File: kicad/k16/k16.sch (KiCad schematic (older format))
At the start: 327 parts, among them J1 PCIEPWR, J3 PINHD-1X4, J5 PINHD-1X4, Q1 NDS351AN, U1 AVALON, U10 AVALON, U11 AVALON, U12 AVALON, U13 AVALON, U14 AVALON, U15 AVALON, U16 AVALON, U17 PIC16LF1459, U18 IR3895, U19 IR3895, U2 AVALON, U20 MCP16321, U21 NL27WZ14, U22 AP7217D / RT9166A, U23 AP7172D / RT9166A, U24 74AUP1G02, U3 AVALON, U4 AVALON, U5 AVALON, U6 AVALON, U7 AVALON, U8 AVALON, U9 AVALON, X1 ASMDB

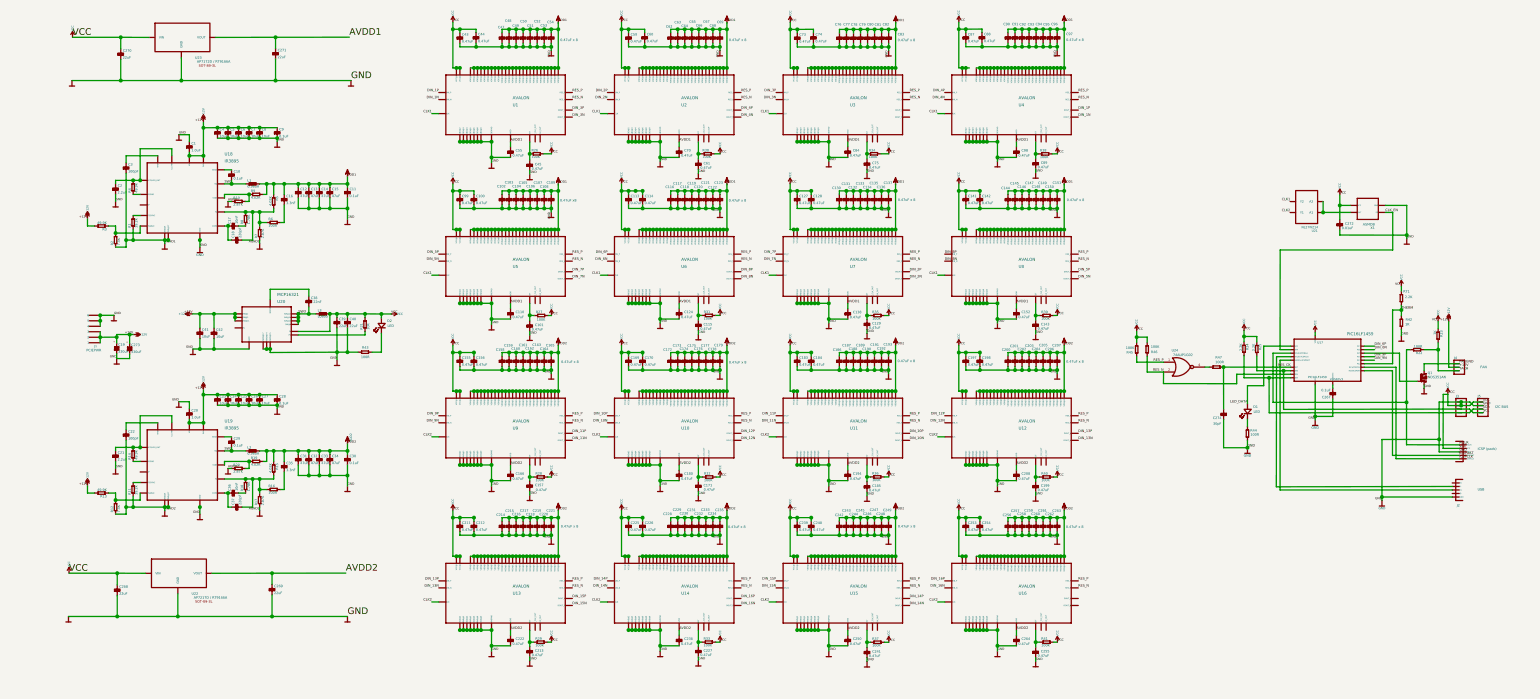
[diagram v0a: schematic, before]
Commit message: update K16 brd for PIC VCC fix, 0.2.1
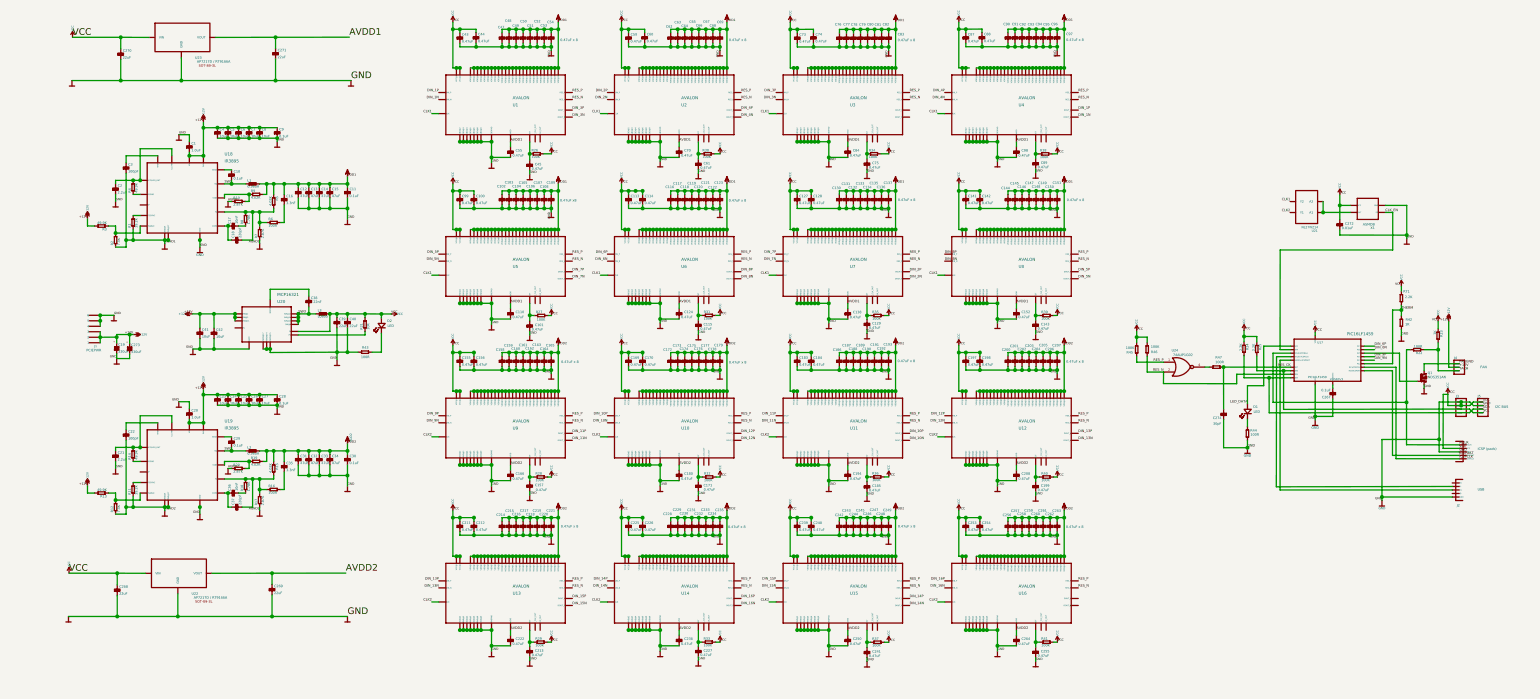
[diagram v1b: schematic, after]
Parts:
- U23: value AP7172D / RT9166A -> AP7217D / RT9166A
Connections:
- net VCC: now also U17.1 (VDD)
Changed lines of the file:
@@
-EESchema Schematic File Version 2  date Thu 30 May 2013 09:22:30 AM ICT
+EESchema Schematic File Version 2  date Fri 21 Jun 2013 07:32:08 AM ICT
 LIBS:k16
 LIBS:power
@@
 encoding utf-8
 Sheet 1 1
-Title "asic-v1.sch"
-Date "30 may 2013"
+Title "Klondike 16 ASIC Miner"
+Date "21 jun 2013"
 Rev ""
 Comp ""
@@
 L VDD1 #VDD061
 U 1 1 517F6E0B
-P 6647 2641
-F 0 "#VDD061" V 6615 2610 22  0001 L BNN
-F 1 "VDD1" H 6647 2641 60  0001 C CNN
-F 2 "" H 6647 2641 60  0001 C CNN
-F 3 "" H 6647 2641 60  0001 C CNN
-	1    6647 2641
+P 6647 2631
+F 0 "#VDD061" V 6615 2600 22  0001 L BNN
+F 1 "VDD1" H 6647 2631 60  0001 C CNN
+F 2 "" H 6647 2631 60  0001 C CNN
+F 3 "" H 6647 2631 60  0001 C CNN
+	1    6647 2631
 	1    0    0    -1
 $EndComp
@@
 L VDD1 #VDD062
 U 1 1 517F6E07
-P 6647 4113
-F 0 "#VDD062" V 6615 4082 22  0001 L BNN
-F 1 "VDD1" H 6647 4113 60  0001 C CNN
-F 2 "" H 6647 4113 60  0001 C CNN
-F 3 "" H 6647 4113 60  0001 C CNN
-	1    6647 4113
+P 6647 4103
+F 0 "#VDD062" V 6615 4072 22  0001 L BNN
+F 1 "VDD1" H 6647 4103 60  0001 C CNN
+F 2 "" H 6647 4103 60  0001 C CNN
+F 3 "" H 6647 4103 60  0001 C CNN
+	1    6647 4103
 	1    0    0    -1
 $EndComp
@@
 L VDD1 #VDD063
 U 1 1 517F6E06
-P 8183 4113
-F 0 "#VDD063" V 8151 4082 22  0001 L BNN
-F 1 "VDD1" H 8183 4113 60  0001 C CNN
-F 2 "" H 8183 4113 60  0001 C CNN
-F 3 "" H 8183 4113 60  0001 C CNN
-	1    8183 4113
+P 8183 4103
+F 0 "#VDD063" V 8151 4072 22  0001 L BNN
+F 1 "VDD1" H 8183 4103 60  0001 C CNN
+F 2 "" H 8183 4103 60  0001 C CNN
+F 3 "" H 8183 4103 60  0001 C CNN
+	1    8183 4103
 	1    0    0    -1
 $EndComp
@@
 L VDD1 #VDD064
 U 1 1 517F6DF8
-P 9719 4113
-F 0 "#VDD064" V 9687 4082 22  0001 L BNN
-F 1 "VDD1" H 9719 4113 60  0001 C CNN
-F 2 "" H 9719 4113 60  0001 C CNN
-F 3 "" H 9719 4113 60  0001 C CNN
-	1    9719 4113
+P 9719 4103
+F 0 "#VDD064" V 9687 4072 22  0001 L BNN
+F 1 "VDD1" H 9719 4103 60  0001 C CNN
+F 2 "" H 9719 4103 60  0001 C CNN
+F 3 "" H 9719 4103 60  0001 C CNN
+	1    9719 4103
 	1    0    0    -1
 $EndComp
@@
 L VDD1 #VDD065
 U 1 1 517F6E04
-P 11255 4113
-F 0 "#VDD065" V 11223 4082 22  0001 L BNN
-F 1 "VDD1" H 11255 4113 60  0001 C CNN
-F 2 "" H 11255 4113 60  0001 C CNN
-F 3 "" H 11255 4113 60  0001 C CNN
-	1    11255 4113
+P 11255 4103
+F 0 "#VDD065" V 11223 4072 22  0001 L BNN
+F 1 "VDD1" H 11255 4103 60  0001 C CNN
+F 2 "" H 11255 4103 60  0001 C CNN
+F 3 "" H 11255 4103 60  0001 C CNN
+	1    11255 4103
 	1    0    0    -1
 $EndComp
@@
 L VDD1 #VDD0104
 U 1 1 518D82F1
-P 8183 2641
-F 0 "#VDD0104" V 8151 2610 22  0001 L BNN
-F 1 "VDD1" H 8183 2641 60  0001 C CNN
-F 2 "" H 8183 2641 60  0001 C CNN
-F 3 "" H 8183 2641 60  0001 C CNN
-	1    8183 2641
+P 8183 2631
+F 0 "#VDD0104" V 8151 2600 22  0001 L BNN
+F 1 "VDD1" H 8183 2631 60  0001 C CNN
+F 2 "" H 8183 2631 60  0001 C CNN
+F 3 "" H 8183 2631 60  0001 C CNN
+	1    8183 2631
 	1    0    0    -1
 $EndComp
@@
 L VDD1 #VDD0107
 U 1 1 518D8547
-P 9720 2642
-F 0 "#VDD0107" V 9688 2611 22  0001 L BNN
-F 1 "VDD1" H 9720 2642 60  0001 C CNN
-F 2 "" H 9720 2642 60  0001 C CNN
-F 3 "" H 9720 2642 60  0001 C CNN
-	1    9720 2642
+P 9720 2632
+F 0 "#VDD0107" V 9688 2601 22  0001 L BNN
+F 1 "VDD1" H 9720 2632 60  0001 C CNN
+F 2 "" H 9720 2632 60  0001 C CNN
+F 3 "" H 9720 2632 60  0001 C CNN
+	1    9720 2632
 	1    0    0    -1
 $EndComp
@@
 L VDD1 #VDD0110
 U 1 1 518D879D
-P 11255 2640
-F 0 "#VDD0110" V 11223 2609 22  0001 L BNN
-F 1 "VDD1" H 11255 2640 60  0001 C CNN
-F 2 "" H 11255 2640 60  0001 C CNN
-F 3 "" H 11255 2640 60  0001 C CNN
-	1    11255 2640
+P 11255 2630
+F 0 "#VDD0110" V 11223 2599 22  0001 L BNN
+F 1 "VDD1" H 11255 2630 60  0001 C CNN
+F 2 "" H 11255 2630 60  0001 C CNN
+F 3 "" H 11255 2630 60  0001 C CNN
+	1    11255 2630
 	1    0    0    -1
 $EndComp
@@
 P 3224 2819
 F 0 "U23" H 3369 2634 22  0000 C CNN
-F 1 "AP7172D / RT9166A" H 3508 2599 22  0000 C CNN
+F 1 "AP7217D / RT9166A" H 3508 2599 22  0000 C CNN
 F 2 "~" H 3224 2819 60  0000 C CNN
 F 3 "~" H 3224 2819 60  0000 C CNN
@@
 	15068 6140 14981 6140
 Wire Wire Line
-	14950 6172 14981 6140
+	14981 6140 14950 6172
 Wire Wire Line
 	15068 6172 14983 6173
 Wire Wire Line
-	14950 6140 14983 6173
+	14983 6173 14950 6140
 Wire Wire Line
-	14670 6140 14870 6140
+	14950 6140 14870 6140
 Wire Wire Line
-	14870 6140 14950 6140
+	14870 6140 14670 6140
 Wire Wire Line
-	14749 6172 14870 6172
+	14950 6172 14870 6172
 Wire Wire Line
-	14870 6172 14950 6172
+	14870 6172 14749 6172
 Connection ~ 14870 6140
 Connection ~ 14870 6172
@@
 	9720 2746 9720 2682
 Wire Wire Line
-	9720 2746 9719 3097
+	9719 3097 9720 2746
 Wire Wire Line
 	9208 2778 9208 2746
@@
 	12535 5822 12578 5822
 Connection ~ 12706 5822
+Text Label 13541 5503 0    22   ~ 0
+VCC
 $EndSCHEMATC

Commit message: update resistors, parts list, v0.2.2
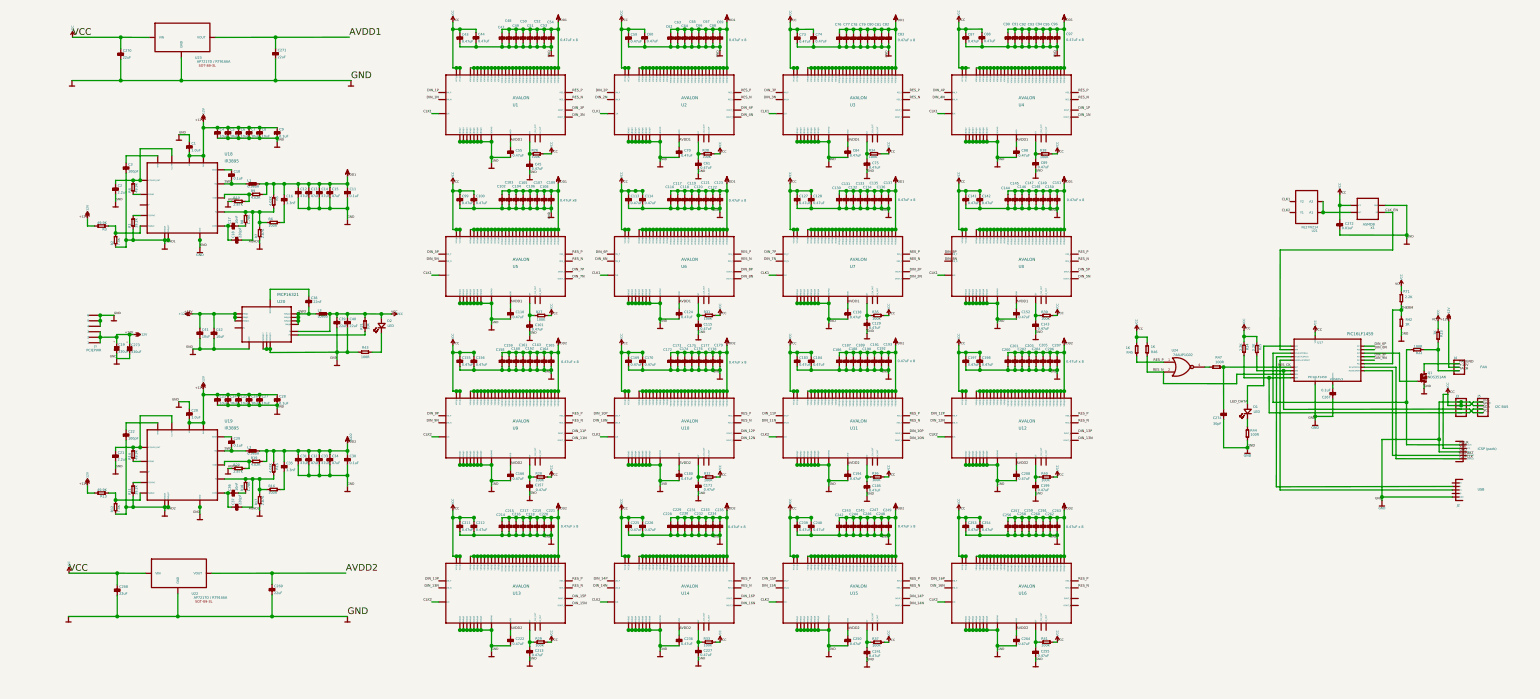
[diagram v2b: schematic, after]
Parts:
- R45, R46: value 100K -> 1K

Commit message: beta final 0.3.0 release
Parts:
- removed U24: 74AUP1G02, ~, symbol 74AUP1G02
- added C275: 0.01uF, symbol C-EU
- added C276: 0.1uF, symbol C-EU
- added D3: SL02, ~, symbol DIODE
- added L10, L11, L12, L13, L14, L15, L16, L17, L18, L19, L4, L5, L6, L7, L8, L9: FB, symbol R-EU
- added L20, L22: 120R @ 100 MHz, symbol R-EU
- added L21: 120R / 100 MHz, symbol R-EU
- added L23: 220R / 100 MHz, symbol R-EU
- added R48: 1K, symbol R-EU
- added unit 1 of U21
- added U24: 74AUP2G02, ~, symbol 74AUP2G02
- added U25: NL27WZ14, symbol NL27WZ14
- C109: value 0.47uF x8 -> 0.47uF
- C123, C137, C151, C165, C179, C193, C207, C221, C235, C249, C263, C54, C69, C83, C97: value 0.47uF x 8 -> 0.47uF
- U21: symbol NL27W -> NL27WZ14
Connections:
- net +12V: now also D3.2 (K)
- net AVDD1: now also L10.1, L11.1, L4.1, L5.1, L6.1, L7.1, L8.1, L9.1; no longer C110.1, C124.1, C138.1, C152.1, C55.1, C70.1, C84.1, C98.1, U1.P$42 (AVDD), U2.P$42 (AVDD), U3.P$42 (AVDD), U4.P$42 (AVDD), U5.P$42 (AVDD), U6.P$42 (AVDD), U7.P$42 (AVDD), U8.P$42 (AVDD)
- net AVDD2: now also L12.1, L13.1, L14.1, L15.1, L16.1, L17.1, L18.1, L19.1; no longer C166.1, C180.1, C194.1, C208.1, C222.1, C236.1, C250.1, C264.1, U10.P$42 (AVDD), U11.P$42 (AVDD), U12.P$42 (AVDD), U13.P$42 (AVDD), U14.P$42 (AVDD), U15.P$42 (AVDD), U16.P$42 (AVDD), U9.P$42 (AVDD)
- net CLK2: now also U21.6; no longer U21.6 (Y1)
- net FANGND: now also D3.1 (A)
- net GND: now also C275.2, C276.1, L22.1, L23.1, R48.2, U21.2 (GND), U24.4 (GND), U24.4 (GND), U25.2 (GND), U25.2 (GND); no longer J2.5 (GND), J2.S1 (GND), J2.S2 (GND), J2.S3 (GND), J2.S4 (GND)
- net RES_CK: now also U25.4; no longer C274.2, R47.2
- net RES_N: now also U24.2 (B), U25.1; no longer U17.12 (RB5)
- net RES_P: now also U24.1 (A)
- net VCC: now also C275.1, C276.2, U21.5 (VCC), U24.8 (VCC), U24.8 (VCC), U25.5 (VCC), U25.5 (VCC)
- net at U21.3, X1.3 (OUT): now also U21.1; no longer U21.1 (A1)
- net at U17.18 (RA1/D-/ICSPCLK): now also L20.1; no longer J2.2 (D-)
- net at U17.19 (RA0/D+/ICSPDAT): now also L21.1; no longer J2.3 (D+)
- net at Q1.3 (G), U17.5 (RC5): now also R48.1
- net at R47.1: now also C274.2, U24.5 (A)
- new net: C222.1, L16.2, U13.P$42 (AVDD)
- new net: C208.1, L15.2, U12.P$42 (AVDD)
- new net: C194.1, L14.2, U11.P$42 (AVDD)
- new net: C180.1, L13.2, U10.P$42 (AVDD)
- new net: C166.1, L12.2, U9.P$42 (AVDD)
- new net: C152.1, L11.2, U8.P$42 (AVDD)
- new net: C138.1, L10.2, U7.P$42 (AVDD)
- new net: C124.1, L9.2, U6.P$42 (AVDD)
- new net: C110.1, L8.2, U5.P$42 (AVDD)
- new net: C98.1, L7.2, U4.P$42 (AVDD)
- new net: C84.1, L6.2, U3.P$42 (AVDD)
- new net: C70.1, L5.2, U2.P$42 (AVDD)
- new net: C55.1, L4.2, U1.P$42 (AVDD)
- new net: C236.1, L17.2, U14.P$42 (AVDD)
- new net: C264.1, L19.2, U16.P$42 (AVDD)
- new net: C250.1, L18.2, U15.P$42 (AVDD)
- new net: J2.5 (GND), J2.S1 (GND), J2.S2 (GND), J2.S3 (GND), J2.S4 (GND), L22.2, L23.2
- new net: U24.3 (Y), U25.3
- new net D+: J2.3 (D+), L21.2
- new net D-: J2.2 (D-), L20.2
- new net RES_DI: U17.12 (RB5), U25.6
- new net RES_PN: R47.2, U24.6 (B), U24.7 (Y)
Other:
- moved on the sheet: C1, C10, C100, C101, C102, C103, C104, C105, C106, C107, C108, C109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
